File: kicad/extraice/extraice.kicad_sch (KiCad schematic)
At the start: 66 parts, among them J1 Conn_01x03, J10 Conn_01x02, J2 Conn_01x03, J3 EncSide, J4 MainSide, J5 Conn_01x05, J6 EncSide, J7 MainSide, J8 Conn_01x02, J9 Conn_01x02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

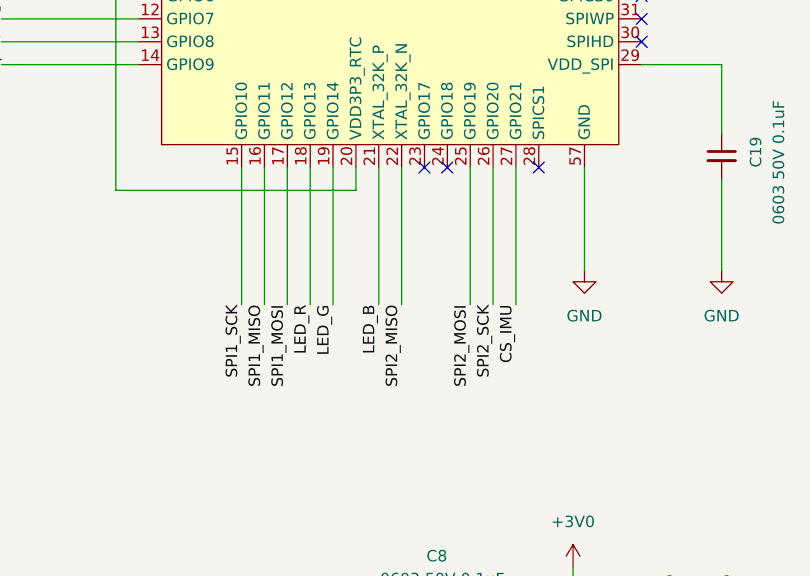
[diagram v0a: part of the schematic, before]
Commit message: Change some GPIO assignments
Signed-off-by: Kazuki Iida <elkel53930@gmail.com>
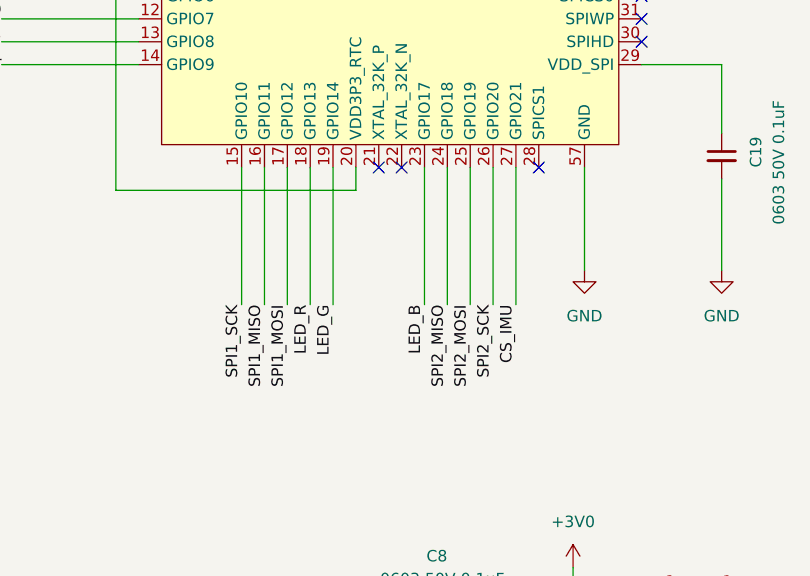
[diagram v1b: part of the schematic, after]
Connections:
- net LED_B: now also U7.23 (GPIO17); no longer U7.21 (XTAL_32K_P)
- net SPI2_MISO: now also U7.24 (GPIO18); no longer U7.22 (XTAL_32K_N)
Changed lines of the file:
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@@
   (no_connect (at 196.85 240.03))
   (no_connect (at 393.7 218.44))
+  (no_connect (at 229.87 162.56))
   (no_connect (at 256.54 143.51))
+  (no_connect (at 227.33 162.56))
   (no_connect (at 196.85 245.11))
   (no_connect (at 256.54 133.35))
@@
   (no_connect (at 308.61 212.09))
   (no_connect (at 256.54 135.89))
-  (no_connect (at 232.41 162.56))
   (no_connect (at 200.66 118.11))
-  (no_connect (at 234.95 162.56))
   (no_connect (at 44.45 41.91))
   (no_connect (at 232.41 106.68))
@@
     (stroke (width 0) (type default))
   )
-  (wire (pts (xy 227.33 162.56) (xy 227.33 177.8))
+  (wire (pts (xy 232.41 162.56) (xy 232.41 177.8))
     (stroke (width 0) (type default))
   )
@@
     (stroke (width 0) (type default))
   )
-  (wire (pts (xy 229.87 177.8) (xy 229.87 162.56))
+  (wire (pts (xy 234.95 177.8) (xy 234.95 162.56))
     (stroke (width 0) (type default))
   )
@@
     (effects (font (size 1.27 1.27)) (justify right bottom))
   )
-  (label "SPI2_MISO" (at 229.87 177.8 270) (fields_autoplaced)
+  (label "SPI2_MISO" (at 234.95 177.8 270) (fields_autoplaced)
     (effects (font (size 1.27 1.27)) (justify right bottom))
   )
@@
     (effects (font (size 1.27 1.27)) (justify left bottom))
   )
-  (label "LED_B" (at 227.33 177.8 270) (fields_autoplaced)
-    (effects (font (size 1.27 1.27)) (justify right bottom))
-  )
+  (label "LED_B" (at 232.41 177.8 270) (fields_autoplaced)
+    (effects (font (size 1.27 1.27)) (justify right bottom))
+  )
